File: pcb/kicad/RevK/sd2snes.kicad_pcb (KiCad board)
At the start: 2 copper layers, 101.5 x 83 mm, 148 parts, among them J101 SNESCART_EXT, J411 Hirose DM1AA, J421 USB Mini-B SMT, P113 CONN_1, P401 CONN_7X2, P402 CONN_2, P403 CONN_2, P404 CONN_3X2, Q101 2N2222A, Q301 IRLML6402PbF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

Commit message: Fix tracing again, fixing other stuff in Schema
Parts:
- moved JP401 0.07 mm to (121.8, 107.4)
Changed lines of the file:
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@@
   )
   (layers
-    (0 Component signal hide)
-    (31 Copper signal)
+    (0 Component signal)
+    (31 Copper signal hide)
     (32 B.Adhes user hide)
     (33 F.Adhes user hide)
@@
   )
   (module Jumper:SolderJumper-2_P1.3mm_Open_Pad1.0x1.5mm (layer Component)
-    (at 121.8565 107.3785 270)
+    (at 121.793 107.3554 270)
     (descr "SMD Solder Jumper, 1x1.5mm Pads, 0.3mm gap, open")
     (tags "solder jumper open")

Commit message: Change N2222A footprint to EBC as per original schematic
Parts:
- Q101, Q511: footprint Package_TO_SOT_SMD:SOT-23 -> mypackages:SOT-23-EBC
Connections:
- Q101 pad 1: Net-(C123-Pad1) -> GND
- Q101 pad 3: GND -> Net-(C123-Pad1)
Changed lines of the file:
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@@
   )
   (layers
-    (0 Component signal)
-    (31 Copper signal hide)
+    (0 Component signal hide)
+    (31 Copper signal)
     (32 B.Adhes user hide)
     (33 F.Adhes user hide)
@@
     (uvia_drill 0.127)
   )
+  (module mypackages:SOT-23-EBC (layer Copper)
+    (at 142.4305 119.6975 270)
+    (descr "SOT-23, Standard")
+    (tags SOT-23)
+    (attr smd)
+    (fp_text reference Q101 (at 1.2065 -0.0635 180) (layer B.SilkS)
+      (effects (font (size 0.5 1) (thickness 0.125)) (justify mirror))
+    )
+    (fp_text value 2N2222A (at 0 -2.5 270) (layer B.Fab)
+      (effects (font (size 1 1) (thickness 0.15)) (justify mirror))
+    )
+    (fp_text user %R (at 0 0 180) (layer B.Fab)
+      (effects (font (size 0.5 0.5) (thickness 0.075)) (justify mirror))
+    )
+    (fp_line (start -0.7 0.95) (end -0.7 -1.5) (layer B.Fab) (width 0.1))
+    (fp_line (start -0.15 1.52) (end 0.7 1.52) (layer B.Fab) (width 0.1))
+    (fp_line (start -0.7 0.95) (end -0.15 1.52) (layer B.Fab) (width 0.1))
+    (fp_line (start 0.7 1.52) (end 0.7 -1.52) (layer B.Fab) (width 0.1))
+    (fp_line (start -0.7 -1.52) (end 0.7 -1.52) (layer B.Fab) (width 0.1))
+    (fp_line (start 0.76 -1.58) (end 0.76 -0.65) (layer B.SilkS) (width 0.12))
+    (fp_line (start 0.76 1.58) (end 0.76 0.65) (layer B.SilkS) (width 0.12))
+    (fp_line (start -1.7 1.75) (end 1.7 1.75) (layer B.CrtYd) (width 0.05))
+    (fp_line (start 1.7 1.75) (end 1.7 -1.75) (layer B.CrtYd) (width 0.05))
+    (fp_line (start 1.7 -1.75) (end -1.7 -1.75) (layer B.CrtYd) (width 0.05))
+    (fp_line (start -1.7 -1.75) (end -1.7 1.75) (layer B.CrtYd) (width 0.05))
+    (fp_line (start 0.76 1.58) (end -1.4 1.58) (layer B.SilkS) (width 0.12))
+    (fp_line (start 0.76 -1.58) (end -0.7 -1.58) (layer B.SilkS) (width 0.12))
+    (pad 2 smd rect (at -1 0.95 270) (size 0.9 0.8) (layers Copper B.Paste B.Mask)
+      (net 307 "Net-(Q101-Pad2)"))
+    (pad 1 smd rect (at -1 -0.95 270) (size 0.9 0.8) (layers Copper B.Paste B.Mask)
+      (net 87 GND))
+    (pad 3 smd rect (at 1 0 270) (size 0.9 0.8) (layers Copper B.Paste B.Mask)
+      (net 306 "Net-(C123-Pad1)"))
+    (model ${KISYS3DMOD}/Package_TO_SOT_SMD.3dshapes/SOT-23.wrl
+      (at (xyz 0 0 0))
+      (scale (xyz 1 1 1))
+      (rotate (xyz 0 0 0))
+    )
+  )
+  (module mypackages:SOT-23-EBC (layer Component)
+    (at 138.684 62.1665 90)
+    (descr "SOT-23, Standard")
+    (tags SOT-23)
+    (attr smd)
+    (fp_text reference Q511 (at 1.2065 0.0635 180) (layer F.SilkS)
+      (effects (font (size 0.5 1) (thickness 0.125)))
+    )
+    (fp_text value 2N2222A (at 0 2.5 90) (layer F.Fab)
+      (effects (font (size 1 1) (thickness 0.15)))
+    )
+    (fp_text user %R (at 0 0 180) (layer F.Fab)
+      (effects (font (size 0.5 0.5) (thickness 0.075)))
+    )
+    (fp_line (start -0.7 -0.95) (end -0.7 1.5) (layer F.Fab) (width 0.1))
+    (fp_line (start -0.15 -1.52) (end 0.7 -1.52) (layer F.Fab) (width 0.1))
+    (fp_line (start -0.7 -0.95) (end -0.15 -1.52) (layer F.Fab) (width 0.1))
+    (fp_line (start 0.7 -1.52) (end 0.7 1.52) (layer F.Fab) (width 0.1))
+    (fp_line (start -0.7 1.52) (end 0.7 1.52) (layer F.Fab) (width 0.1))
+    (fp_line (start 0.76 1.58) (end 0.76 0.65) (layer F.SilkS) (width 0.12))
+    (fp_line (start 0.76 -1.58) (end 0.76 -0.65) (layer F.SilkS) (width 0.12))
+    (fp_line (start -1.7 -1.75) (end 1.7 -1.75) (layer F.CrtYd) (width 0.05))
+    (fp_line (start 1.7 -1.75) (end 1.7 1.75) (layer F.CrtYd) (width 0.05))
+    (fp_line (start 1.7 1.75) (end -1.7 1.75) (layer F.CrtYd) (width 0.05))
+    (fp_line (start -1.7 1.75) (end -1.7 -1.75) (layer F.CrtYd) (width 0.05))
+    (fp_line (start 0.76 -1.58) (end -1.4 -1.58) (layer F.SilkS) (width 0.12))
+    (fp_line (start 0.76 1.58) (end -0.7 1.58) (layer F.SilkS) (width 0.12))
+    (pad 2 smd rect (at -1 -0.95 90) (size 0.9 0.8) (layers Component F.Paste F.Mask)
+      (net 305 "Net-(Q511-Pad2)"))
+    (pad 1 smd rect (at -1 0.95 90) (size 0.9 0.8) (layers Component F.Paste F.Mask)
+      (net 87 GND))
+    (pad 3 smd rect (at 1 0 90) (size 0.9 0.8) (layers Component F.Paste F.Mask)
+      (net 9 /Memory/RAM_/CE))
+    (model ${KISYS3DMOD}/Package_TO_SOT_SMD.3dshapes/SOT-23.wrl
+      (at (xyz 0 0 0))
+      (scale (xyz 1 1 1))
+      (rotate (xyz 0 0 0))
+    )
+  )
   (module Package_SO:TSSOP-8_4.4x3mm_P0.65mm (layer Component)
     (at 104.381201 112.975401)
@@
     (model ${KISYS3DMOD}/Package_TO_SOT_SMD.3dshapes/SOT-23.wrl
       (at (xyz 0 0 0))
-      (scale (xyz 1 1 1))
-      (rotate (xyz 0 0 0))
-    )
-  )
-  (module Package_TO_SOT_SMD:SOT-23 (layer Component)
-    (at 138.684 62.1665 90)
-    (descr "SOT-23, Standard")
-    (tags SOT-23)
-    (attr smd)
-    (fp_text reference Q511 (at 1.2065 0.0635 180) (layer F.SilkS)
-      (effects (font (size 0.5 1) (thickness 0.125)))
-    )
-    (fp_text value 2N2222A (at 0 2.5 90) (layer F.Fab)
-      (effects (font (size 1 1) (thickness 0.15)))
-    )
-    (fp_line (start 0.76 1.58) (end -0.7 1.58) (layer F.SilkS) (width 0.12))
-    (fp_line (start 0.76 -1.58) (end -1.4 -1.58) (layer F.SilkS) (width 0.12))
-    (fp_line (start -1.7 1.75) (end -1.7 -1.75) (layer F.CrtYd) (width 0.05))
-    (fp_line (start 1.7 1.75) (end -1.7 1.75) (layer F.CrtYd) (width 0.05))
-    (fp_line (start 1.7 -1.75) (end 1.7 1.75) (layer F.CrtYd) (width 0.05))
-    (fp_line (start -1.7 -1.75) (end 1.7 -1.75) (layer F.CrtYd) (width 0.05))
-    (fp_line (start 0.76 -1.58) (end 0.76 -0.65) (layer F.SilkS) (width 0.12))
-    (fp_line (start 0.76 1.58) (end 0.76 0.65) (layer F.SilkS) (width 0.12))
-    (fp_line (start -0.7 1.52) (end 0.7 1.52) (layer F.Fab) (width 0.1))
-    (fp_line (start 0.7 -1.52) (end 0.7 1.52) (layer F.Fab) (width 0.1))
-    (fp_line (start -0.7 -0.95) (end -0.15 -1.52) (layer F.Fab) (width 0.1))
-    (fp_line (start -0.15 -1.52) (end 0.7 -1.52) (layer F.Fab) (width 0.1))
-    (fp_line (start -0.7 -0.95) (end -0.7 1.5) (layer F.Fab) (width 0.1))
-    (fp_text user %R (at 0 0 180) (layer F.Fab)
-      (effects (font (size 0.5 0.5) (thickness 0.075)))
-    )
-    (pad 3 smd rect (at 1 0 90) (size 0.9 0.8) (layers Component F.Paste F.Mask)
-      (net 9 /Memory/RAM_/CE))
-    (pad 2 smd rect (at -1 0.95 90) (size 0.9 0.8) (layers Component F.Paste F.Mask)
-      (net 305 "Net-(Q511-Pad2)"))
-    (pad 1 smd rect (at -1 -0.95 90) (size 0.9 0.8) (layers Component F.Paste F.Mask)
-      (net 87 GND))
-    (model ${KISYS3DMOD}/Package_TO_SOT_SMD.3dshapes/SOT-23.wrl
-      (at (xyz 0 0 0))
-      (scale (xyz 1 1 1))
-      (rotate (xyz 0 0 0))
-    )
-  )
-  (module Package_TO_SOT_SMD:SOT-23 (layer Copper)
-    (at 142.4305 119.6975 270)
-    (descr "SOT-23, Standard")
-    (tags SOT-23)
-    (attr smd)
-    (fp_text reference Q101 (at 0 2.5 270) (layer B.SilkS)
-      (effects (font (size 1 1) (thickness 0.15)) (justify mirror))
-    )
-    (fp_text value 2N2222A (at 0 -2.5 270) (layer B.Fab)
-      (effects (font (size 1 1) (thickness 0.15)) (justify mirror))
-    )
-    (fp_line (start 0.76 -1.58) (end -0.7 -1.58) (layer B.SilkS) (width 0.12))
-    (fp_line (start 0.76 1.58) (end -1.4 1.58) (layer B.SilkS) (width 0.12))
-    (fp_line (start -1.7 -1.75) (end -1.7 1.75) (layer B.CrtYd) (width 0.05))
-    (fp_line (start 1.7 -1.75) (end -1.7 -1.75) (layer B.CrtYd) (width 0.05))
-    (fp_line (start 1.7 1.75) (end 1.7 -1.75) (layer B.CrtYd) (width 0.05))
-    (fp_line (start -1.7 1.75) (end 1.7 1.75) (layer B.CrtYd) (width 0.05))
-    (fp_line (start 0.76 1.58) (end 0.76 0.65) (layer B.SilkS) (width 0.12))
-    (fp_line (start 0.76 -1.58) (end 0.76 -0.65) (layer B.SilkS) (width 0.12))
-    (fp_line (start -0.7 -1.52) (end 0.7 -1.52) (layer B.Fab) (width 0.1))
-    (fp_line (start 0.7 1.52) (end 0.7 -1.52) (layer B.Fab) (width 0.1))
-    (fp_line (start -0.7 0.95) (end -0.15 1.52) (layer B.Fab) (width 0.1))
-    (fp_line (start -0.15 1.52) (end 0.7 1.52) (layer B.Fab) (width 0.1))
-    (fp_line (start -0.7 0.95) (end -0.7 -1.5) (layer B.Fab) (width 0.1))
-    (fp_text user %R (at 0 0 180) (layer B.Fab)
-      (effects (font (size 0.5 0.5) (thickness 0.075)) (justify mirror))
-    )
-    (pad 3 smd rect (at 1 0 270) (size 0.9 0.8) (layers Copper B.Paste B.Mask)
-      (net 87 GND))
-    (pad 2 smd rect (at -1 -0.95 270) (size 0.9 0.8) (layers Copper B.Paste B.Mask)
-      (net 307 "Net-(Q101-Pad2)"))
-    (pad 1 smd rect (at -1 0.95 270) (size 0.9 0.8) (layers Copper B.Paste B.Mask)
-      (net 306 "Net-(C123-Pad1)"))
-    (model ${KISYS3DMOD}/Package_TO_SOT_SMD.3dshapes/SOT-23.wrl
-      (at (xyz 0 0 0))

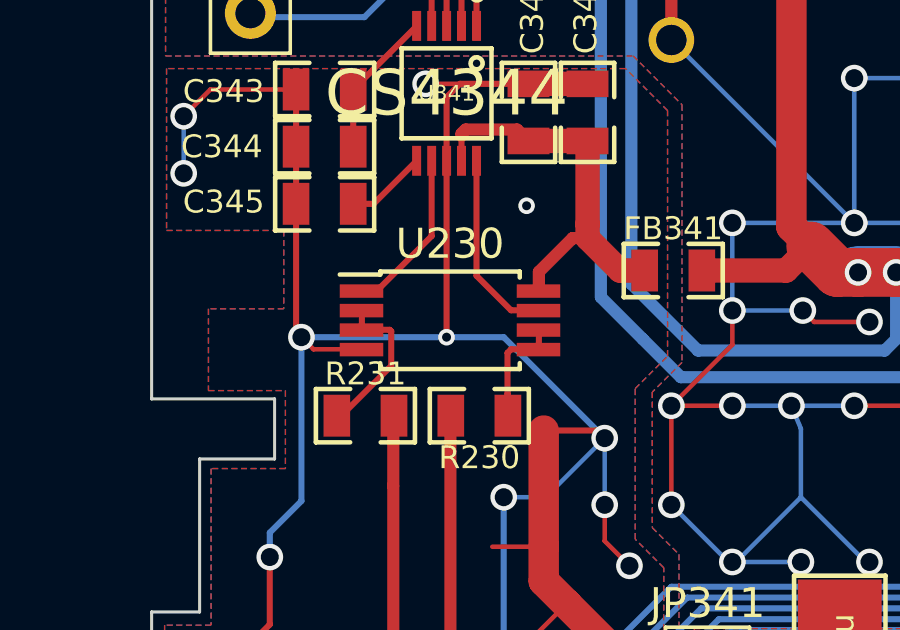
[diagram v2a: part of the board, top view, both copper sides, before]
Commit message: Fix OpAmp orientation
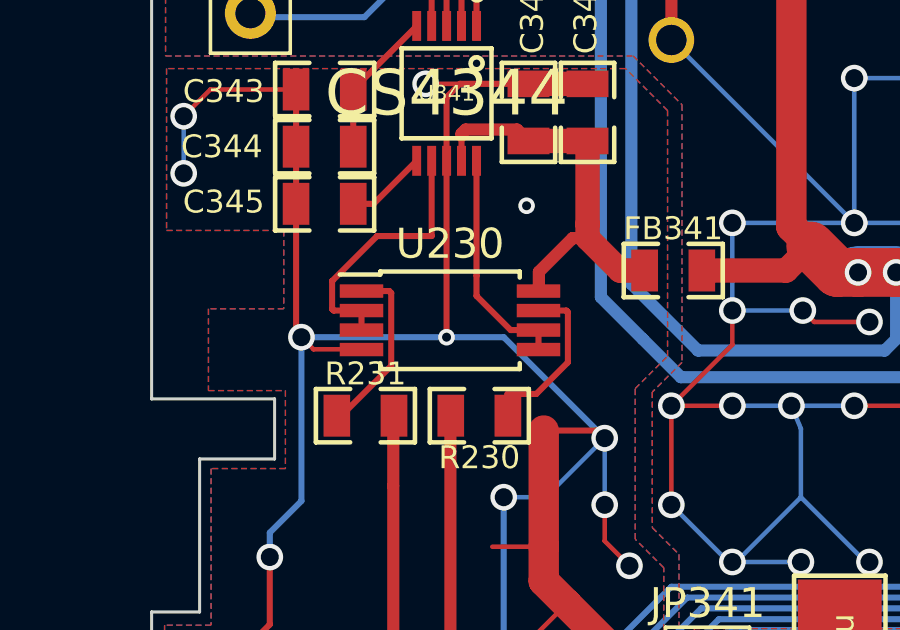
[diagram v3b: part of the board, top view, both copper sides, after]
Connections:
- U230 pad 1: Net-(U230-Pad1) -> Net-(R231-Pad1)
- U230 pad 2: Net-(R231-Pad1) -> Net-(U230-Pad2)
- U230 pad 3: Net-(R231-Pad1) -> Net-(U230-Pad2)
- U230 pad 5: Net-(R230-Pad1) -> Net-(U230-Pad5)
- U230 pad 6: Net-(R230-Pad1) -> Net-(U230-Pad5)
- U230 pad 7: Net-(U230-Pad7) -> Net-(R230-Pad1)
- U341 pad 10: Net-(U230-Pad7) -> Net-(U230-Pad5)
- U341 pad 7: Net-(U230-Pad1) -> Net-(U230-Pad2)
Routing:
- net Net-(U230-Pad2): track 0.00 -> 9.03 mm
- net Net-(U230-Pad5): track 0.00 -> 7.69 mm
- net Net-(U230-Pad7): track 6.39 -> 0.00 mm
- net Net-(U230-Pad1): track 5.59 -> 0.00 mm
- net Net-(R230-Pad1): track 4.02 -> 6.03 mm
- net Net-(R231-Pad1): track 5.66 -> 6.80 mm
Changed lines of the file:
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@@
     (thickness 0.8)
     (drawings 242)
-    (tracks 4090)
+    (tracks 4097)
     (zones 0)
     (modules 148)
@@
   )
   (layers
-    (0 Component signal hide)
-    (31 Copper signal)
+    (0 Component signal)
+    (31 Copper signal hide)
     (32 B.Adhes user hide)
     (33 F.Adhes user hide)
@@
   )
   (setup
-    (last_trace_width 0.1524)
+    (last_trace_width 0.2032)
     (user_trace_width 0.14986)
     (user_trace_width 0.1524)
@@
   (net 341 "Net-(U201-Pad55)")
   (net 342 "Net-(U201-Pad54)")
-  (net 343 "Net-(U230-Pad1)")
-  (net 344 "Net-(U230-Pad7)")
-  (net 345 "Net-(R230-Pad1)")
-  (net 346 "Net-(R231-Pad1)")
+  (net 343 "Net-(R230-Pad1)")
+  (net 344 "Net-(R231-Pad1)")
+  (net 345 "Net-(U230-Pad2)")
+  (net 346 "Net-(U230-Pad5)")
   (net_class Default "This is the default net class."
     (clearance 0.1524)
@@
     (add_net "Net-(U201-Pad55)")
     (add_net "Net-(U201-Pad56)")
-    (add_net "Net-(U230-Pad1)")
-    (add_net "Net-(U230-Pad7)")
+    (add_net "Net-(U230-Pad2)")
+    (add_net "Net-(U230-Pad5)")
     (add_net "Net-(U311-Pad4)")
     (add_net "Net-(U321-Pad4)")
@@
     )
     (pad 1 smd rect (at -2.95 -0.975) (size 1.45 0.45) (layers Component F.Paste F.Mask)
-      (net 343 "Net-(U230-Pad1)"))
+      (net 344 "Net-(R231-Pad1)"))
     (pad 2 smd rect (at -2.95 -0.325) (size 1.45 0.45) (layers Component F.Paste F.Mask)
-      (net 346 "Net-(R231-Pad1)"))
+      (net 345 "Net-(U230-Pad2)"))
     (pad 3 smd rect (at -2.95 0.325) (size 1.45 0.45) (layers Component F.Paste F.Mask)
-      (net 346 "Net-(R231-Pad1)"))
+      (net 345 "Net-(U230-Pad2)"))
     (pad 4 smd rect (at -2.95 0.975) (size 1.45 0.45) (layers Component F.Paste F.Mask)
       (net 304 GNDA))
     (pad 5 smd rect (at 2.95 0.975) (size 1.45 0.45) (layers Component F.Paste F.Mask)
-      (net 345 "Net-(R230-Pad1)"))
+      (net 346 "Net-(U230-Pad5)"))
     (pad 6 smd rect (at 2.95 0.325) (size 1.45 0.45) (layers Component F.Paste F.Mask)
-      (net 345 "Net-(R230-Pad1)"))
+      (net 346 "Net-(U230-Pad5)"))
     (pad 7 smd rect (at 2.95 -0.325) (size 1.45 0.45) (layers Component F.Paste F.Mask)
-      (net 344 "Net-(U230-Pad7)"))
+      (net 343 "Net-(R230-Pad1)"))
     (pad 8 smd rect (at 2.95 -0.975) (size 1.45 0.45) (layers Component F.Paste F.Mask)
       (net 5 +3.3VDAC))
@@
       (net 65 AUDIO_L))
     (pad 1 smd rect (at -0.9525 0) (size 0.889 1.397) (layers Component F.Paste F.Mask)
-      (net 346 "Net-(R231-Pad1)"))
+      (net 344 "Net-(R231-Pad1)"))
     (model smd/chip_cms.wrl
       (at (xyz 0 0 0))
@@
     (fp_line (start -1.651 0.889) (end -1.651 -0.889) (layer F.SilkS) (width 0.1524))
     (pad 1 smd rect (at -0.9525 0 180) (size 0.889 1.397) (layers Component F.Paste F.Mask)
-      (net 345 "Net-(R230-Pad1)"))
+      (net 343 "Net-(R230-Pad1)"))
     (pad 2 smd rect (at 0.9525 0 180) (size 0.889 1.397) (layers Component F.Paste F.Mask)
       (net 66 AUDIO_R))
@@
       (net 303 "Net-(C345-Pad1)"))
     (pad 7 smd rect (at 0.49784 -2.2479 180) (size 0.29972 0.99822) (layers Component F.Paste F.Mask)
-      (net 343 "Net-(U230-Pad1)"))
+      (net 345 "Net-(U230-Pad2)"))
     (pad 8 smd rect (at 0 -2.2479 180) (size 0.29972 0.99822) (layers Component F.Paste F.Mask)
       (net 304 GNDA))
@@
       (net 5 +3.3VDAC))
     (pad 10 smd rect (at -0.99822 -2.2479 180) (size 0.29972 0.99822) (layers Component F.Paste F.Mask)
-      (net 344 "Net-(U230-Pad7)"))
+      (net 346 "Net-(U230-Pad5)"))
   )
   (module mypackages:TSSOP48 (layer Component)
@@
   (via (at 127.5715 75.2475) (size 0.55372) (layers Component Copper) (net 334))
   (segment (start 127.5715 75.2475) (end 126.1745 75.2475) (width 0.2032) (layer Component) (net 334))
-  (segment (start 101.944 111.9915) (end 101.444 111.9915) (width 0.2032) (layer Component) (net 343))
-  (segment (start 103.76916 110.16634) (end 101.944 111.9915) (width 0.2032) (layer Component) (net 343))
-  (segment (start 103.76916 107.6579) (end 103.76916 110.16634) (width 0.2032) (layer Component) (net 343))
-  (segment (start 106.4158 112.6415) (end 107.344 112.6415) (width 0.2032) (layer Component) (net 344))
-  (segment (start 105.26522 111.49092) (end 106.4158 112.6415) (width 0.2032) (layer Component) (net 344))
-  (segment (start 105.26522 107.6579) (end 105.26522 111.49092) (width 0.2032) (layer Component) (net 344))
-  (segment (start 107.344 113.2915) (end 107.344 113.9415) (width 0.2032) (layer Component) (net 345))
-  (segment (start 106.299 115.4303) (end 106.299 116.332) (width 0.2032) (layer Component) (net 345))
-  (segment (start 106.299 114.0583) (end 106.299 115.4303) (width 0.2032) (layer Component) (net 345))
-  (segment (start 106.4158 113.9415) (end 106.299 114.0583) (width 0.2032) (layer Component) (net 345))
-  (segment (start 107.344 113.9415) (end 106.4158 113.9415) (width 0.2032) (layer Component) (net 345))
-  (segment (start 101.444 113.2915) (end 101.444 112.6415) (width 0.2032) (layer Component) (net 346))
-  (segment (start 100.584 116.078) (end 100.584 116.332) (width 0.2032) (layer Component) (net 346))
-  (segment (start 102.423001 113.342301) (end 102.423001 114.492999) (width 0.2032) (layer Component) (net 346))
-  (segment (start 102.3722 113.2915) (end 102.423001 113.342301) (width 0.2032) (layer Component) (net 346))
-  (segment (start 101.444 113.2915) (end 102.3722 113.2915) (width 0.2032) (layer Component) (net 346))
-  (segment (start 102.423001 114.492999) (end 100.584 116.332) (width 0.2032) (layer Component) (net 346))
+  (segment (start 101.944 111.9915) (end 101.444 111.9915) (width 0.2032) (layer Component) (net 344))
+  (segment (start 103.76916 107.6579) (end 103.76916 110.16634) (width 0.2032) (layer Component) (net 345))
+  (segment (start 105.26522 107.6579) (end 105.26522 111.49092) (width 0.2032) (layer Component) (net 346))
+  (segment (start 106.299 115.4303) (end 106.299 116.332) (width 0.2032) (layer Component) (net 343))
+  (segment (start 108.310202 112.701202) (end 108.259401 112.650401) (width 0.2032) (layer Component) (net 343))
+  (segment (start 108.259401 112.650401) (end 107.331201 112.650401) (width 0.2032) (layer Component) (net 343))
+  (segment (start 108.310202 114.378602) (end 108.310202 112.701202) (width 0.2032) (layer Component) (net 343))
+  (segment (start 107.258504 115.4303) (end 108.310202 114.378602) (width 0.2032) (layer Component) (net 343))
+  (segment (start 106.299 115.4303) (end 107.258504 115.4303) (width 0.2032) (layer Component) (net 343))
+  (segment (start 100.584 116.078) (end 100.584 116.332) (width 0.2032) (layer Component) (net 344))
+  (segment (start 102.423001 114.492999) (end 100.584 116.332) (width 0.2032) (layer Component) (net 344))
+  (segment (start 102.359401 112.000401) (end 101.431201 112.000401) (width 0.2032) (layer Component) (net 344))
+  (segment (start 102.423001 112.064001) (end 102.359401 112.000401) (width 0.2032) (layer Component) (net 344))
+  (segment (start 102.423001 114.492999) (end 102.423001 112.064001) (width 0.2032) (layer Component) (net 344))
+  (segment (start 101.431201 113.300401) (end 101.431201 112.650401) (width 0.2032) (layer Component) (net 345))
+  (segment (start 101.94906 110.16634) (end 103.76916 110.16634) (width 0.2032) (layer Component) (net 345))
+  (segment (start 100.4522 111.6632) (end 101.94906 110.16634) (width 0.2032) (layer Component) (net 345))
+  (segment (start 100.4522 112.5996) (end 100.4522 111.6632) (width 0.2032) (layer Component) (net 345))
+  (segment (start 100.503001 112.650401) (end 100.4522 112.5996) (width 0.2032) (layer Component) (net 345))
+  (segment (start 101.431201 112.650401) (end 100.503001 112.650401) (width 0.2032) (layer Component) (net 345))
+  (segment (start 107.331201 113.950401) (end 107.331201 113.300401) (width 0.2032) (layer Component) (net 346))
+  (segment (start 106.403001 113.300401) (end 105.26522 112.16262) (width 0.2032) (layer Component) (net 346))
+  (segment (start 105.26522 112.16262) (end 105.26522 111.49092) (width 0.2032) (layer Component) (net 346))
+  (segment (start 107.331201 113.300401) (end 106.403001 113.300401) (width 0.2032) (layer Component) (net 346))
   (zone (net 87) (net_name GND) (layer Component) (hatch edge 0.508)
     (connect_pads (clearance 0.1905))
